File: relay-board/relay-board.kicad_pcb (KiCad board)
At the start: 2 copper layers, 107 x 181.5 mm, 60 parts, among them J1 Conn_01x02, J2 Conn_01x02, J3 Conn_01x02, J4 Conn_01x02, J5 Conn_01x02, J6 Conn_01x02, J7 Conn_01x02, J8 Conn_01x02, Q1 PN2222A, Q2 PN2222A, Q3 PN2222A, Q4 PN2222A, Q5 PN2222A, Q6 PN2222A, Q7 PN2222A, Q8 PN2222A, U1 FOD814A, U10 RT114, U11 FOD814A, U12 RT114, U13 FOD814A, U14 RT114, U15 FOD814A, U16 RT114, U2 RT114, U3 FOD814A, U4 RT114, U5 FOD814A, U6 RT114, U7 FOD814A, U8 RT114, U9 FOD814A

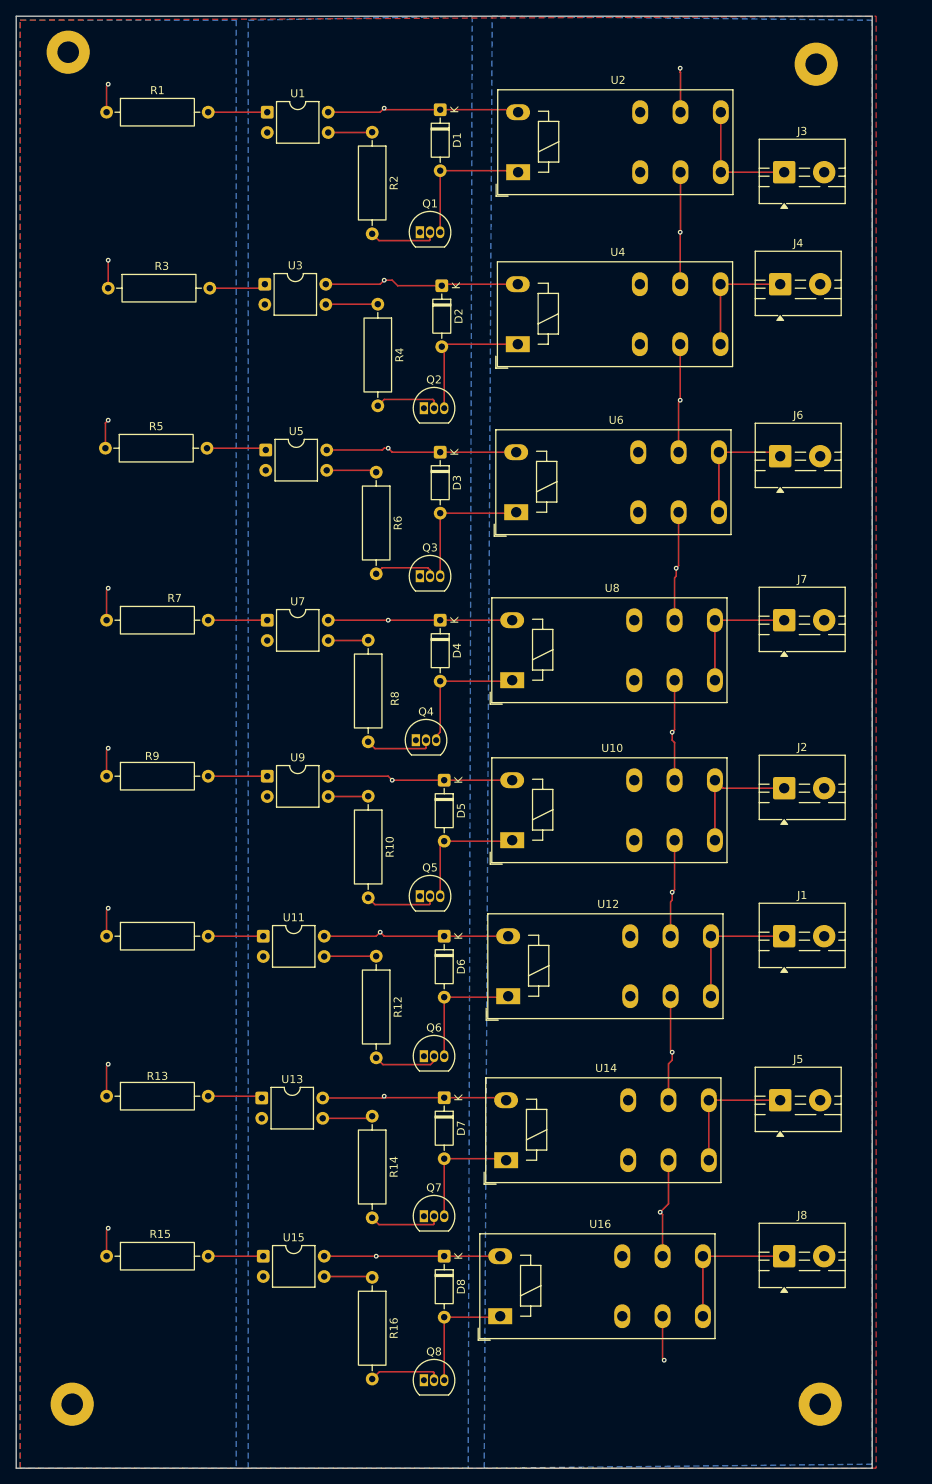
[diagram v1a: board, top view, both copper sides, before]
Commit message: relay-board: finish routing pcb
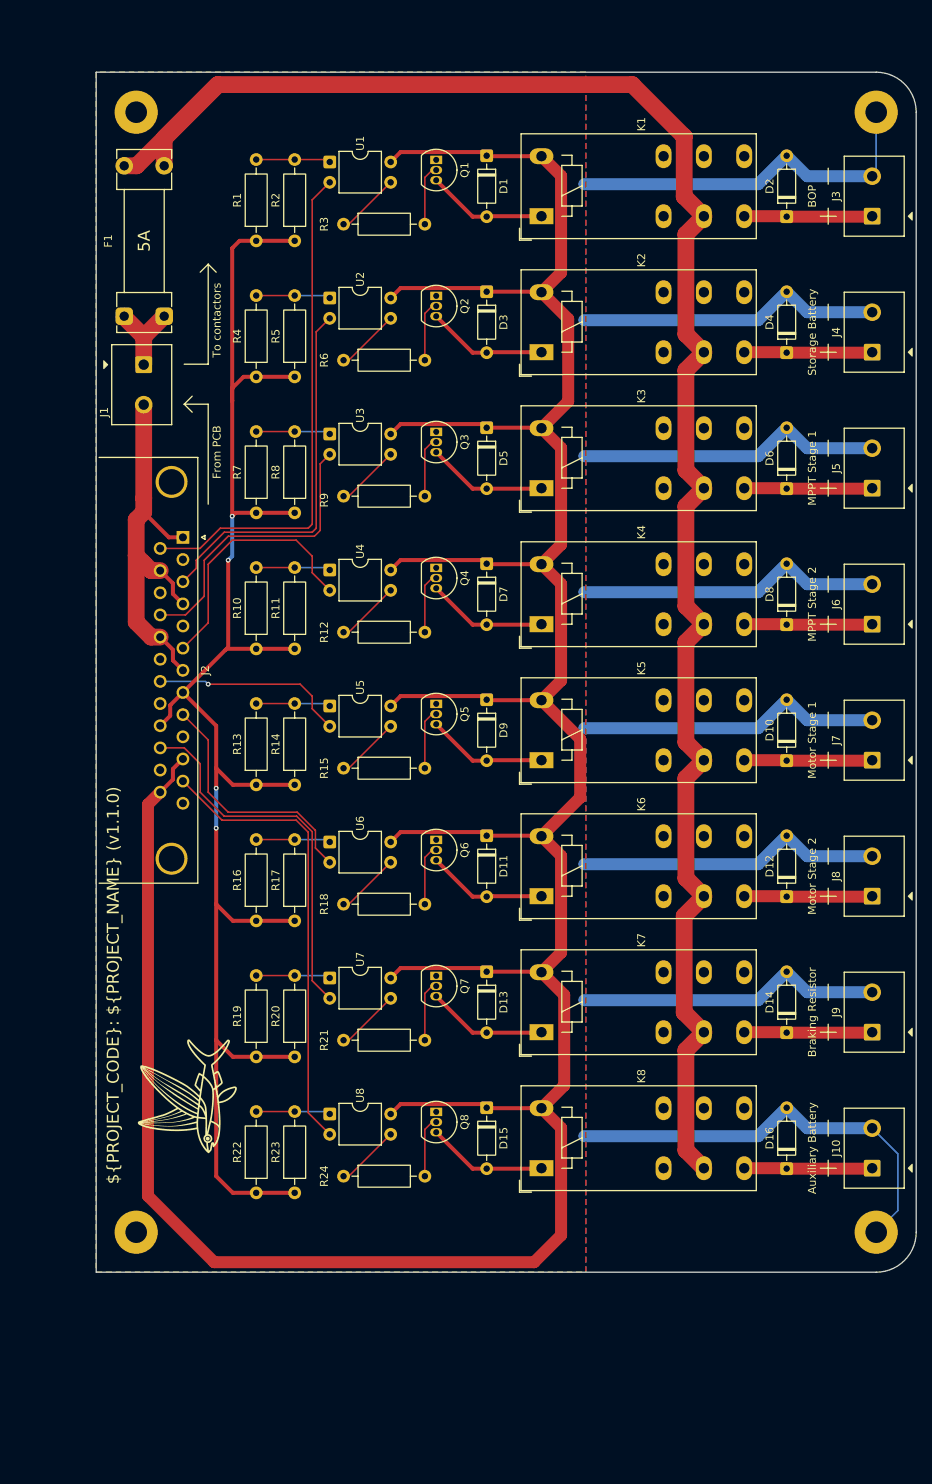
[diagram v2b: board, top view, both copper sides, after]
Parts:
- removed U10, U12, U14, U16: RT114, Relay_THT:Relay_DPDT_Schrack-RT2-FormC_RM5mm
- removed U11, U13, U15, U9: FOD814A, Package_DIP:DIP-4_W7.62mm
- added D10: 1N4148, Diode_THT:D_DO-35_SOD27_P7.62mm_Horizontal, F.Cu at (116.3, 105.6)
- added D11: 1N4148, Diode_THT:D_DO-35_SOD27_P7.62mm_Horizontal, F.Cu at (78.8, 114.9)
- added D12: 1N4148, Diode_THT:D_DO-35_SOD27_P7.62mm_Horizontal, F.Cu at (116.3, 122.6)
- added D13: 1N4148, Diode_THT:D_DO-35_SOD27_P7.62mm_Horizontal, F.Cu at (78.8, 131.9)
- added D14: 1N4148, Diode_THT:D_DO-35_SOD27_P7.62mm_Horizontal, F.Cu at (116.3, 139.6)
- added D15: 1N4148, Diode_THT:D_DO-35_SOD27_P7.62mm_Horizontal, F.Cu at (78.8, 148.9)
- added D16: 1N4148, Diode_THT:D_DO-35_SOD27_P7.62mm_Horizontal, F.Cu at (116.3, 156.6)
- added D9: 1N4148, Diode_THT:D_DO-35_SOD27_P7.62mm_Horizontal, F.Cu at (78.8, 97.9)
- added F1: Fuse Holder, Fuse:Fuseholder_Clip-5x20mm_Littelfuse_111_Lateral_P18.80x5.00mm_D1.17mm_Horizontal, F.Cu at (33.5, 50.0)
- added J10: Contactor Output, Exocet:Wurth_Term_Blk_2pos_Side_Entry_5mm, F.Cu at (127.0, 154.0)
- added J9: Contactor Output, Exocet:Wurth_Term_Blk_2pos_Side_Entry_5mm, F.Cu at (127.0, 137.0)
- added K1: RTD14005, Relay_THT:Relay_DPDT_Schrack-RT2-FormC_RM5mm, F.Cu at (85.7, 37.5)
- added K2: RTD14005, Relay_THT:Relay_DPDT_Schrack-RT2-FormC_RM5mm, F.Cu at (85.7, 54.5)
- added K3: RTD14005, Relay_THT:Relay_DPDT_Schrack-RT2-FormC_RM5mm, F.Cu at (85.7, 71.5)
- added K4: RTD14005, Relay_THT:Relay_DPDT_Schrack-RT2-FormC_RM5mm, F.Cu at (85.7, 88.5)
- added K5: RTD14005, Relay_THT:Relay_DPDT_Schrack-RT2-FormC_RM5mm, F.Cu at (85.7, 105.5)
- added K6: RTD14005, Relay_THT:Relay_DPDT_Schrack-RT2-FormC_RM5mm, F.Cu at (85.7, 122.5)
- added K7: RTD14005, Relay_THT:Relay_DPDT_Schrack-RT2-FormC_RM5mm, F.Cu at (85.7, 139.5)
- added K8: RTD14005, Relay_THT:Relay_DPDT_Schrack-RT2-FormC_RM5mm, F.Cu at (85.7, 156.5)
- added R17: 1.2k, Resistor_THT:R_Axial_DIN0207_L6.3mm_D2.5mm_P10.16mm_Horizontal, F.Cu at (54.8, 125.6)
- added R18: 1.2k, Resistor_THT:R_Axial_DIN0207_L6.3mm_D2.5mm_P10.16mm_Horizontal, F.Cu at (60.9, 123.5)
- added R19: 1.2k, Resistor_THT:R_Axial_DIN0207_L6.3mm_D2.5mm_P10.16mm_Horizontal, F.Cu at (50.0, 142.6)
- added R20: 1.2k, Resistor_THT:R_Axial_DIN0207_L6.3mm_D2.5mm_P10.16mm_Horizontal, F.Cu at (54.8, 142.6)
- added R21: 1.2k, Resistor_THT:R_Axial_DIN0207_L6.3mm_D2.5mm_P10.16mm_Horizontal, F.Cu at (60.9, 140.5)
- added R22: 1.2k, Resistor_THT:R_Axial_DIN0207_L6.3mm_D2.5mm_P10.16mm_Horizontal, F.Cu at (50.0, 159.6)
- added R23: 1.2k, Resistor_THT:R_Axial_DIN0207_L6.3mm_D2.5mm_P10.16mm_Horizontal, F.Cu at (54.8, 159.6)
- added R24: 1.2k, Resistor_THT:R_Axial_DIN0207_L6.3mm_D2.5mm_P10.16mm_Horizontal, F.Cu at (60.9, 157.5)
- J1: value Conn_01x02 -> 24V Select; footprint TerminalBlock:TerminalBlock_MaiXu_MX126-5.0-02P_1x02_P5.00mm -> Exocet:Wurth_Term_Blk_2pos_Side_Entry_5mm
- J2: value Conn_01x02 -> RA25P; footprint TerminalBlock:TerminalBlock_MaiXu_MX126-5.0-02P_1x02_P5.00mm -> Connector_Dsub:DSUB-25_Pins_Horizontal_P2.77x2.84mm_EdgePinOffset7.70mm_Housed_MountingHolesOffset9.12mm
- J3, J4, J5, J6, J7, J8: value Conn_01x02 -> Contactor Output; footprint TerminalBlock:TerminalBlock_MaiXu_MX126-5.0-02P_1x02_P5.00mm -> Exocet:Wurth_Term_Blk_2pos_Side_Entry_5mm
- Q1, Q2, Q3, Q4, Q5, Q6, Q7, Q8: value PN2222A -> PN2222ATA
- R1, R10, R11, R12, R13, R14, R15, R16, R2, R3, R4, R5, R6, R7, R8, R9: footprint Resistor_THT:R_Axial_DIN0309_L9.0mm_D3.2mm_P12.70mm_Horizontal -> Resistor_THT:R_Axial_DIN0207_L6.3mm_D2.5mm_P10.16mm_Horizontal
- U2, U4, U6, U8: value RT114 -> FOD814A; footprint Relay_THT:Relay_DPDT_Schrack-RT2-FormC_RM5mm -> Package_DIP:DIP-4_W7.62mm
- moved J1 105.7 mm to (35.9, 58.6), turned to -90 degrees
- moved D8 89.8 mm to (116.3, 88.6), turned to 90 degrees
- moved J2 81.4 mm to (40.8, 77.6), turned to -90 degrees
- moved J5 79.8 mm to (127.0, 69.0), turned to 90 degrees
- moved D6 70.4 mm to (116.3, 71.6), turned to 90 degrees
- moved R15 67.8 mm to (60.9, 106.5)
- moved D7 67.0 mm to (78.8, 80.9)
- moved U8 58.8 mm to (59.2, 149.7)
- moved D4 54.7 mm to (116.3, 54.6), turned to 90 degrees
- moved J8 48.8 mm to (127.0, 120.0), turned to 90 degrees
- moved U6 47.4 mm to (59.2, 115.7)
- moved R16 46.9 mm to (50.0, 125.6), turned to 90 degrees
- moved R9 45.9 mm to (60.9, 72.5)
- moved U7 45.4 mm to (59.2, 132.7)
- moved D5 44.4 mm to (78.8, 63.9)
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- renumbered H2 to H1, H1 to H2
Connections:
- D1 pad 1: VCC 5V -> +5V
- D2 pad 1: VCC 5V -> Net-(D2-K)
- D2 pad 2: Net-(D2-A) -> GND
- D3 pad 1: VCC 5V -> +5V
- D4 pad 1: VCC 5V -> Net-(D4-K)
- D4 pad 2: Net-(D4-A) -> GND
- D5 pad 1: VCC 5V -> +5V
- D6 pad 1: VCC 5V -> Net-(D6-K)
- D6 pad 2: Net-(D6-A) -> GND
- D7 pad 1: VCC 5V -> +5V
- D8 pad 1: VCC 5V -> Net-(D8-K)
- D8 pad 2: Net-(D8-A) -> GND
- J1 pad 2: GND -> Net-(J1-Pin_2)
- J2 pad 1: Net-(J2-Pin_1) -> Net-(J1-Pin_2)
- J3 pad 1: Net-(J3-Pin_1) -> Net-(D2-K)
- J4 pad 1: Net-(J4-Pin_1) -> Net-(D4-K)
- J5 pad 1: Net-(J5-Pin_1) -> Net-(D6-K)
- J6 pad 1: Net-(J6-Pin_1) -> Net-(D8-K)
- J7 pad 1: Net-(J7-Pin_1) -> Net-(D10-K)
- Q2 pad 3: Net-(D2-A) -> Net-(D3-A)
- Q3 pad 3: Net-(D3-A) -> Net-(D5-A)
- Q4 pad 3: Net-(D4-A) -> Net-(D7-A)
- Q5 pad 3: Net-(D5-A) -> Net-(D9-A)
- Q6 pad 3: Net-(D6-A) -> Net-(D11-A)
- Q7 pad 3: Net-(D7-A) -> Net-(D13-A)
- Q8 pad 3: Net-(D8-A) -> Net-(D15-A)
- R1 pad 1: VCC 3.3V -> +3.3V
- R10 pad 1: Net-(R10-Pad1) -> +3.3V
- R10 pad 2: Net-(Q5-B) -> Net-(R10-Pad2)
- R11 pad 1: VCC 3.3V -> +3.3V
- R11 pad 2: Net-(R11-Pad2) -> Net-(R10-Pad2)
- R12 pad 2: Net-(Q6-B) -> Net-(Q4-B)
- R13 pad 1: VCC 3.3V -> +3.3V
- R14 pad 1: Net-(R14-Pad1) -> +3.3V
- R14 pad 2: Net-(Q7-B) -> Net-(R13-Pad2)
- R15 pad 1: VCC 3.3V -> Net-(R15-Pad1)
- R15 pad 2: Net-(R15-Pad2) -> Net-(Q5-B)
- R16 pad 1: Net-(R16-Pad1) -> +3.3V
- R16 pad 2: Net-(Q8-B) -> Net-(R16-Pad2)
- R2 pad 1: Net-(R2-Pad1) -> +3.3V
- R2 pad 2: Net-(Q1-B) -> Net-(R1-Pad2)
- R3 pad 1: VCC 3.3V -> Net-(R3-Pad1)
- R3 pad 2: Net-(R3-Pad2) -> Net-(Q1-B)
- R4 pad 1: Net-(R4-Pad1) -> +3.3V
- R4 pad 2: Net-(Q2-B) -> Net-(R4-Pad2)
- R5 pad 1: VCC 3.3V -> +3.3V
- R5 pad 2: Net-(R5-Pad2) -> Net-(R4-Pad2)
- R6 pad 2: Net-(Q3-B) -> Net-(Q2-B)
- R7 pad 1: VCC 3.3V -> +3.3V
- R8 pad 1: Net-(R8-Pad1) -> +3.3V
- R8 pad 2: Net-(Q4-B) -> Net-(R7-Pad2)
- R9 pad 1: VCC 3.3V -> Net-(R9-Pad1)
- R9 pad 2: Net-(R9-Pad2) -> Net-(Q3-B)
- U1 pad 2: /In_BOP -> /BOP_SWITCH
- U1 pad 3: Net-(R2-Pad1) -> Net-(R3-Pad1)
- U1 pad 4: VCC 5V -> +5V
- U3 pad 1: Net-(R3-Pad2) -> Net-(R7-Pad2)
- U3 pad 2: /In_BatterieStockage -> /MPPT_PRECHARGE_STAGE_1
- U3 pad 3: Net-(R4-Pad1) -> Net-(R9-Pad1)
- U3 pad 4: VCC 5V -> +5V
- U5 pad 1: Net-(R5-Pad2) -> Net-(R13-Pad2)
- U5 pad 2: /In_isoFuel -> /MOTOR_PRECHARGE_STAGE_1
- U5 pad 3: Net-(R6-Pad1) -> Net-(R15-Pad1)
- U5 pad 4: VCC 5V -> +5V
- U7 pad 1: Net-(R7-Pad2) -> Net-(R19-Pad2)
- U7 pad 2: /In_IsoFuel2 -> /BRAKING_RESISTOR
- U7 pad 3: Net-(R8-Pad1) -> Net-(R21-Pad1)
- U7 pad 4: VCC 5V -> +5V
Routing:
- net +5V: track 0.00 -> 422.7 mm
- net GND: track 0.00 -> 331.9 mm
- net +24V: track 0.00 -> 242.3 mm
- net +3.3V: track 0.00 -> 203.0 mm, vias 0 -> 4
- net VCC 5V: track 187.6 -> 0.00 mm, vias 8 -> 0
- net VCC 24V: track 103.2 -> 0.00 mm, vias 9 -> 0
- net /BOP_SWITCH: track 0.00 -> 63.9 mm
- net /AUXILIARY_BATTERY_SWITCH: track 0.00 -> 57.2 mm
- net Net-(J1-Pin_2): track 0.00 -> 52.0 mm
- net /BRAKING_RESISTOR: track 0.00 -> 47.2 mm
- net /STORAGE_BATTERY_SWITCH: track 0.00 -> 47.0 mm
- net /MPPT_PRECHARGE_STAGE_1: track 0.00 -> 37.0 mm
- net /MPPT_PRECHARGE_STAGE_2: track 0.00 -> 32.0 mm
- net /MOTOR_PRECHARGE_STAGE_2: track 0.00 -> 31.1 mm
- net VCC 3.3V: track 29.6 -> 0.00 mm, vias 8 -> 0
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- added copper zone on B.Cu, net GND
- removed copper zone on B.Cu, net VCC 24V
- removed copper zone on B.Cu, net VCC 3.3V
- removed copper zone on B.Cu, net VCC 5V
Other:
- board size 107 x 181.5 mm -> 102.5 x 150 mm
- board text added: "${PROJECT_CODE}: ${PROJECT_NAME} (${REVISION})"
- board text added: "5A"
- board text added: "Auxiliary Battery"
- board text added: "BOP"
- board text added: "Braking Resistor"
- board text added: "From PCB"
- board text added: "MPPT Stage 1"
- board text added: "MPPT Stage 2"
- board text added: "Motor Stage 1"
- board text added: "Motor Stage 2"
- board text added: "Storage Battery"
- board text added: "To contactors"

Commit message: relay-board: increase trace width and spacing
Recommendations after a review, to reduce the chance of damaging the PCB
while soldering.
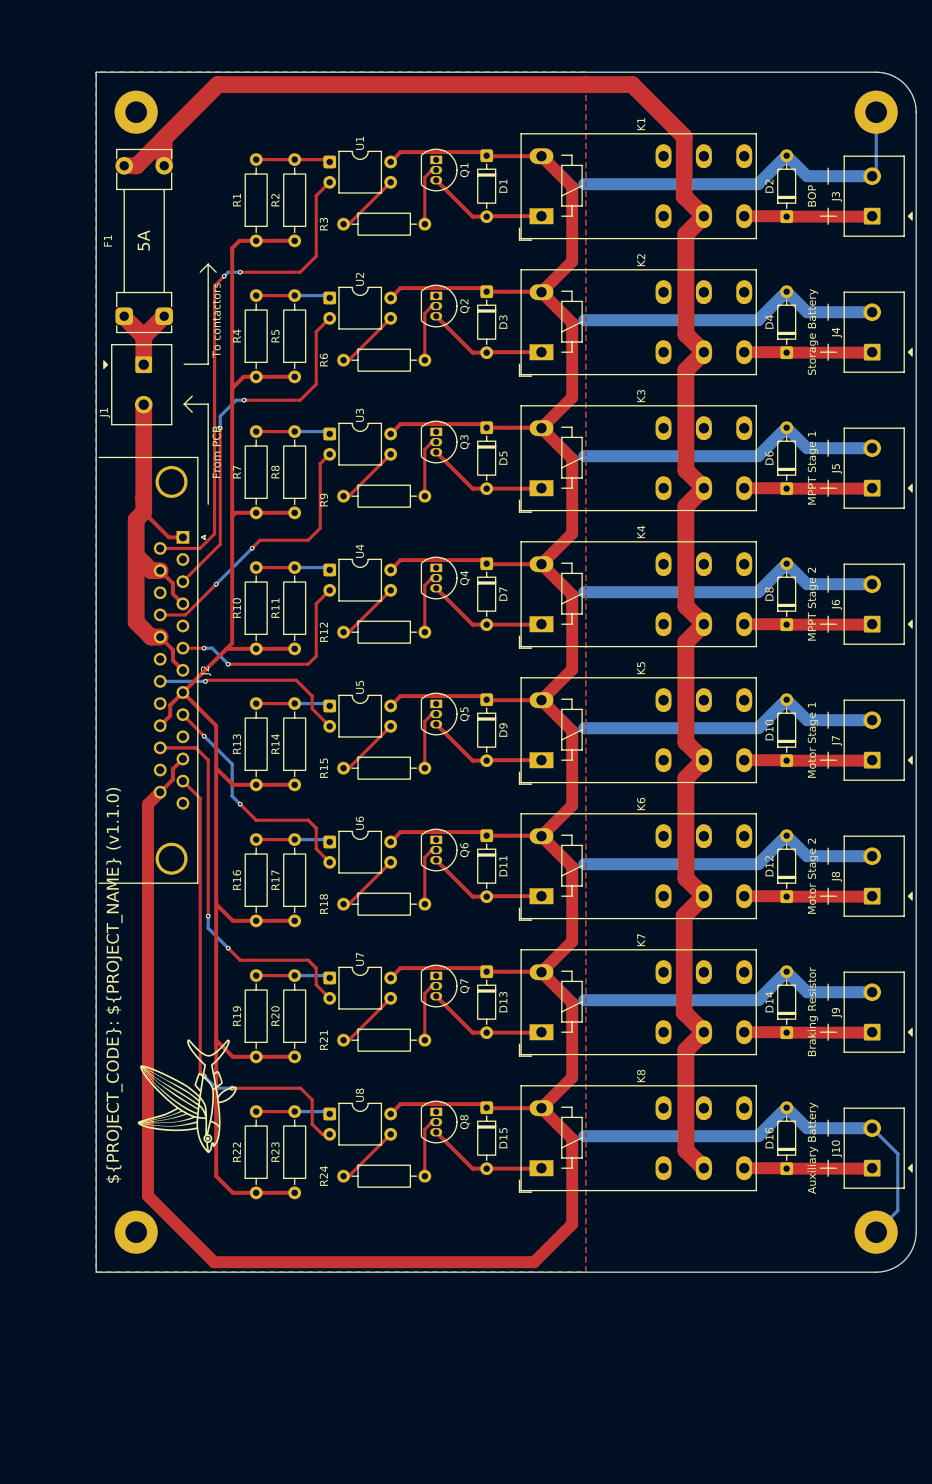
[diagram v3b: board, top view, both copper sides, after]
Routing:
- net +5V: track 422.7 -> 428.8 mm
- net /MPPT_PRECHARGE_STAGE_2: track 32.0 -> 26.8 mm, vias 0 -> 2
- net /MPPT_PRECHARGE_STAGE_1: track 37.0 -> 34.2 mm, vias 0 -> 2
- net /STORAGE_BATTERY_SWITCH: track 47.0 -> 45.2 mm, vias 0 -> 2
- net /AUXILIARY_BATTERY_SWITCH: track 57.2 -> 58.5 mm, vias 0 -> 2
- net /MOTOR_PRECHARGE_STAGE_2: track 31.1 -> 29.9 mm, vias 0 -> 2
- net /BOP_SWITCH: track 63.9 -> 62.7 mm, vias 0 -> 2
- net /BRAKING_RESISTOR: track 47.2 -> 47.7 mm, vias 0 -> 2
- net +3.3V: vias 4 -> 0

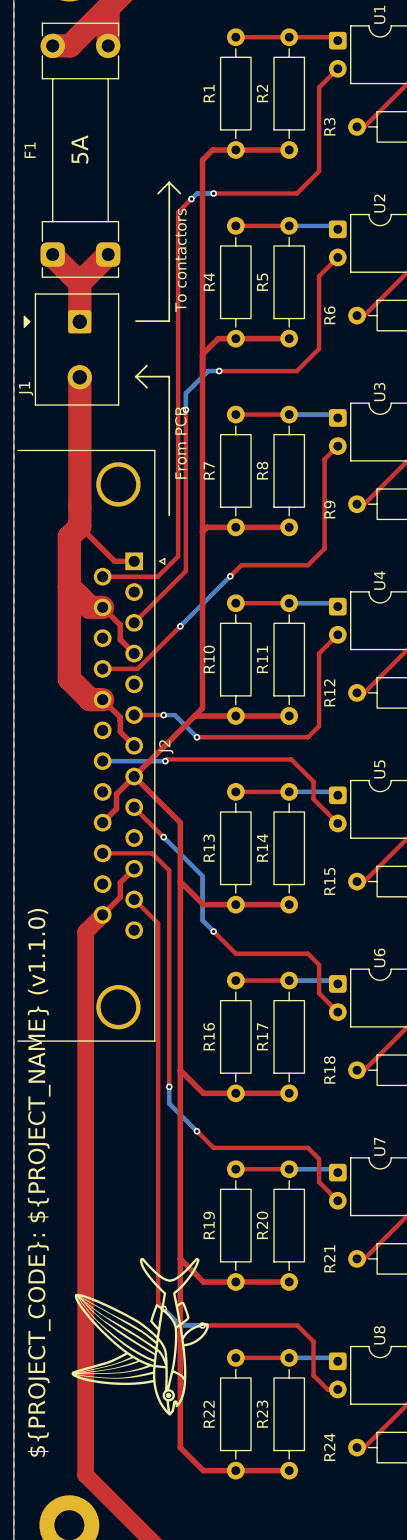
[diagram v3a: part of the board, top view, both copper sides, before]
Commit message: relay-board: remove 3.3V input
Reduces risk of shorts and was not necessary to begin with. Now inputs
are active high, which is also less prone to mistakes on the programming
side.
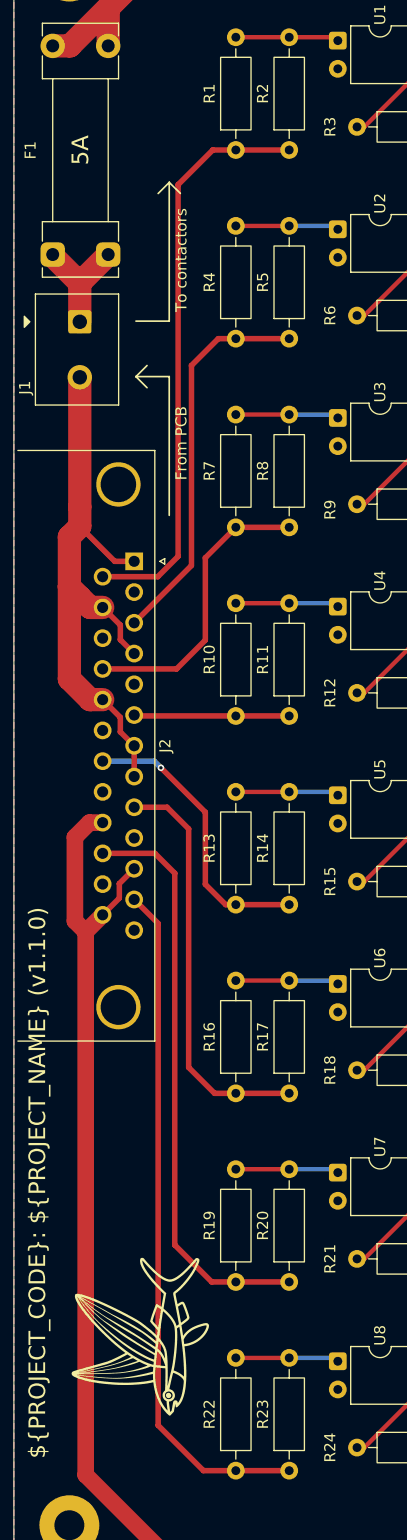
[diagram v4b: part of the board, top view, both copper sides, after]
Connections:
- J2 pad 22: +3.3V -> +5V
- J2 pad 8: +3.3V -> Net-(J1-Pin_2)
- R1 pad 1: +3.3V -> /BOP_SWITCH
- R10 pad 1: +3.3V -> /MPPT_PRECHARGE_STAGE_2
- R11 pad 1: +3.3V -> /MPPT_PRECHARGE_STAGE_2
- R13 pad 1: +3.3V -> /MOTOR_PRECHARGE_STAGE_1
- R14 pad 1: +3.3V -> /MOTOR_PRECHARGE_STAGE_1
- R16 pad 1: +3.3V -> /MOTOR_PRECHARGE_STAGE_2
- R17 pad 1: +3.3V -> /MOTOR_PRECHARGE_STAGE_2
- R19 pad 1: +3.3V -> /BRAKING_RESISTOR
- R2 pad 1: +3.3V -> /BOP_SWITCH
- R20 pad 1: +3.3V -> /BRAKING_RESISTOR
- R22 pad 1: +3.3V -> /AUXILIARY_BATTERY_SWITCH
- R23 pad 1: +3.3V -> /AUXILIARY_BATTERY_SWITCH
- R4 pad 1: +3.3V -> /STORAGE_BATTERY_SWITCH
- R5 pad 1: +3.3V -> /STORAGE_BATTERY_SWITCH
- R7 pad 1: +3.3V -> /MPPT_PRECHARGE_STAGE_1
- R8 pad 1: +3.3V -> /MPPT_PRECHARGE_STAGE_1
- U1 pad 2: /BOP_SWITCH -> GND
- U2 pad 2: /STORAGE_BATTERY_SWITCH -> GND
- U3 pad 2: /MPPT_PRECHARGE_STAGE_1 -> GND
- U4 pad 2: /MPPT_PRECHARGE_STAGE_2 -> GND
- U5 pad 2: /MOTOR_PRECHARGE_STAGE_1 -> GND
- U6 pad 2: /MOTOR_PRECHARGE_STAGE_2 -> GND
- U7 pad 2: /BRAKING_RESISTOR -> GND
- U8 pad 2: /AUXILIARY_BATTERY_SWITCH -> GND
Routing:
- net +3.3V: track 203.0 -> 0.00 mm
- net /MPPT_PRECHARGE_STAGE_2: track 26.8 -> 14.0 mm, vias 2 -> 0
- net +5V: track 428.8 -> 440.8 mm
- net /BOP_SWITCH: track 62.7 -> 52.4 mm, vias 2 -> 0
- net /STORAGE_BATTERY_SWITCH: track 45.2 -> 35.1 mm, vias 2 -> 0
- net /MPPT_PRECHARGE_STAGE_1: track 34.2 -> 26.4 mm, vias 2 -> 0
- net /MOTOR_PRECHARGE_STAGE_2: track 29.9 -> 37.3 mm, vias 2 -> 0
- net /BRAKING_RESISTOR: track 47.7 -> 52.4 mm, vias 2 -> 0
- net /AUXILIARY_BATTERY_SWITCH: track 58.5 -> 61.8 mm, vias 2 -> 0
- net Net-(J1-Pin_2): track 52.0 -> 54.8 mm
- net /MOTOR_PRECHARGE_STAGE_1: track 24.6 -> 26.0 mm

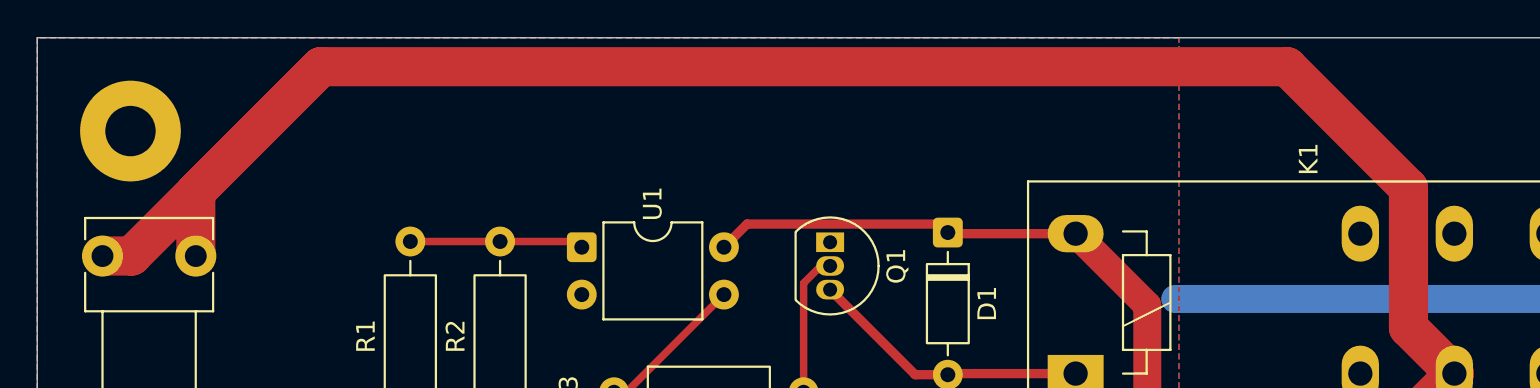
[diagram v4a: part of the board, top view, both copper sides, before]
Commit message: relay-board: finish pcb layout
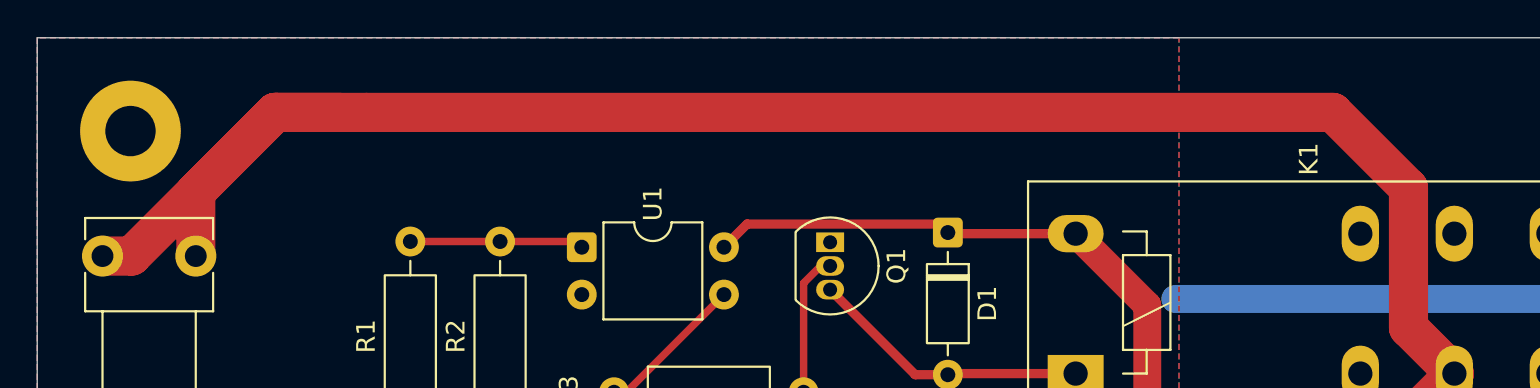
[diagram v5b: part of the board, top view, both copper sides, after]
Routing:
- net +24V: track 242.3 -> 236.9 mm
